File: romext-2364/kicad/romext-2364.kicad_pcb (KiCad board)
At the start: 2 copper layers, 58.4 x 58.4 mm, 2 parts, among them J1 2364, U1 2764

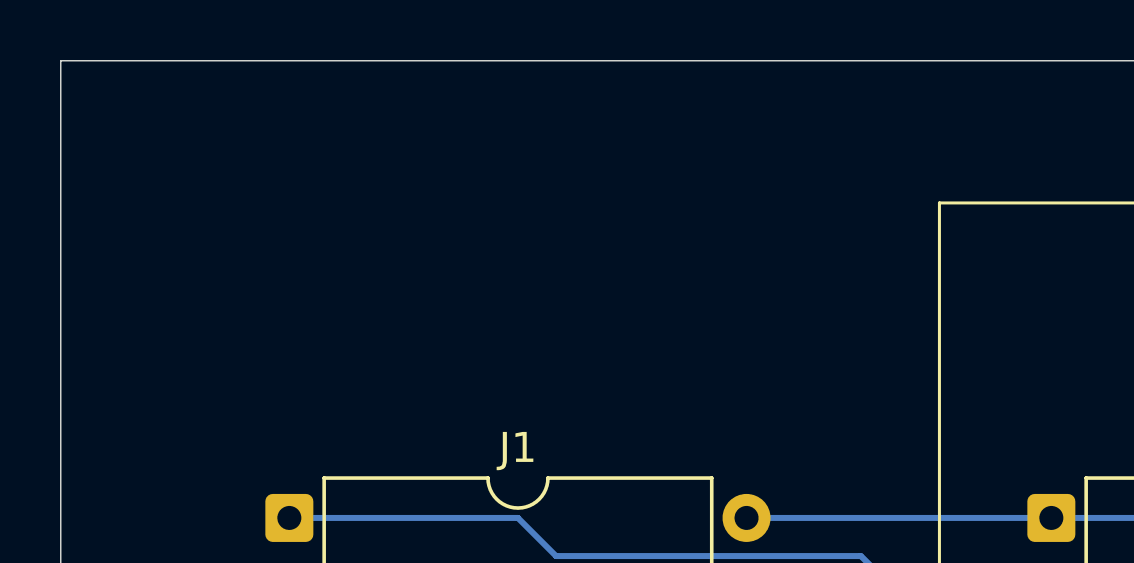
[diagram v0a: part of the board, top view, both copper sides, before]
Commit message: hwdev.romext-2364: Add name, url and revision to title block
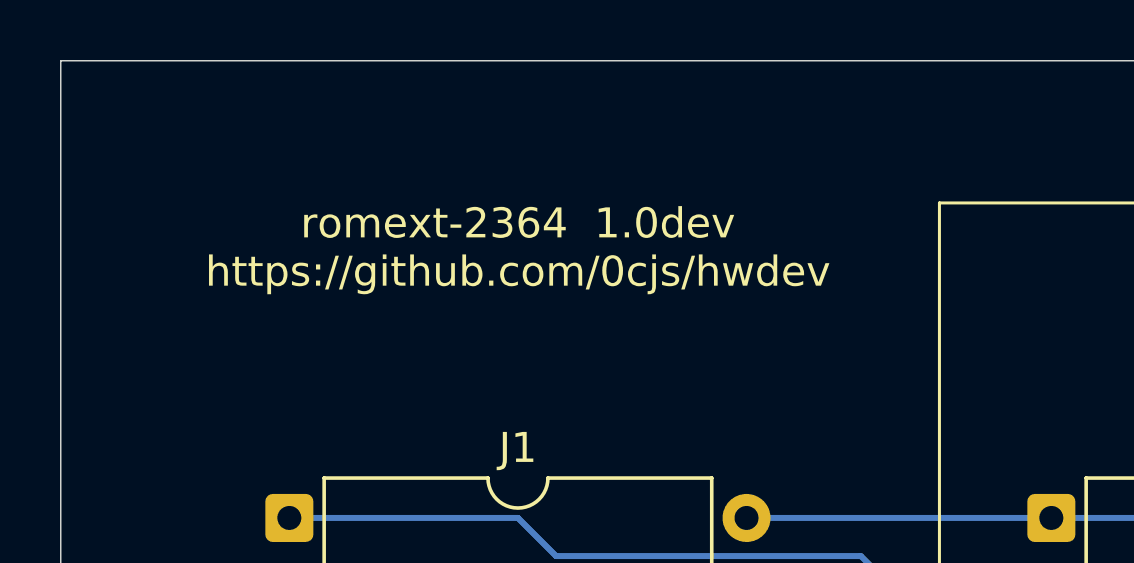
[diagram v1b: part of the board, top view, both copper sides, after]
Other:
- board text added: "${TITLE} ${REVISION} ${COMMENT1}"
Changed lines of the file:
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@@
 	)
 	(paper "A4")
+	(title_block
+		(title "romext-2364")
+		(rev "1.0dev")
+		(comment 1 "https://github.com/0cjs/hwdev")
+	)
 	(layers
 		(0 "F.Cu" signal)
@@
 		(layer "Edge.Cuts")
 	)
+	(gr_text "${TITLE}  ${REVISION}\n${COMMENT1}\n"
+		(at 109.22 43.18 0)
+		(layer "F.SilkS")
+		(effects
+			(font
+				(size 1 1)
+				(thickness 0.1)
+			)
+			(justify bottom)
+		)
+	)
 	(segment

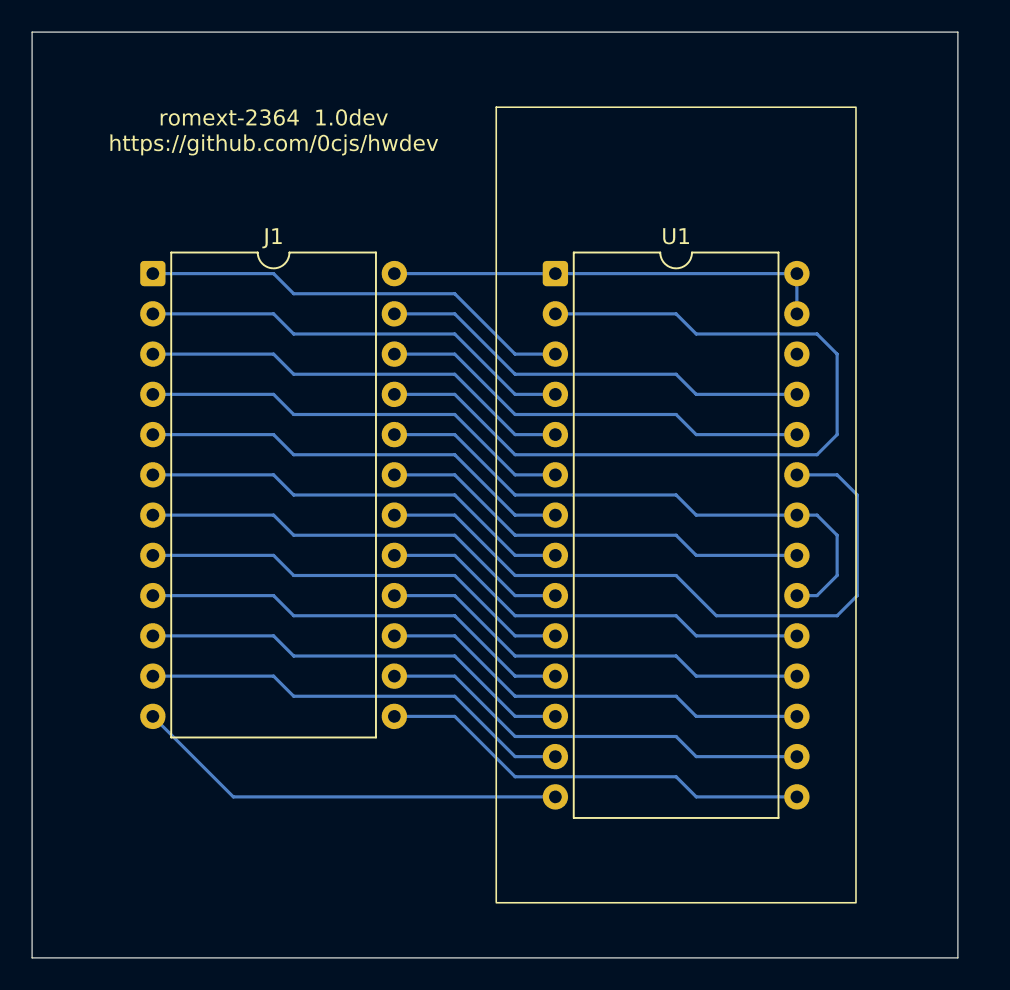
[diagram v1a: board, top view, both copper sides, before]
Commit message: romext-2364 pcb: Resize board; add mounting holes; move title
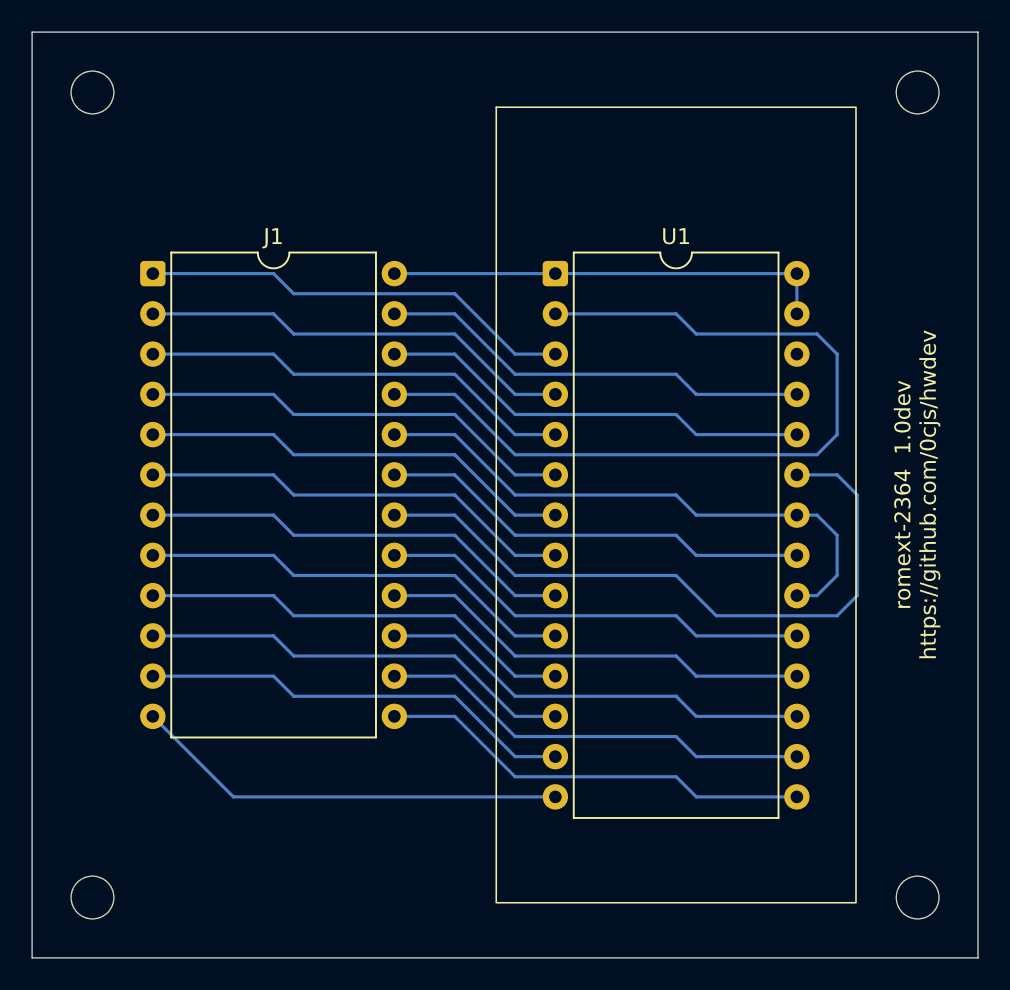
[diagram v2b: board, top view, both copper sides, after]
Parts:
- added REF**: MountingHole_2.7mm_M2.5, MountingHole:MountingHole_2.7mm_M2.5, F.Cu at (149.9, 39.4)
- added REF**: MountingHole_2.7mm_M2.5, MountingHole:MountingHole_2.7mm_M2.5, F.Cu at (149.9, 90.2)
- added REF**: MountingHole_2.7mm_M2.5, MountingHole:MountingHole_2.7mm_M2.5, F.Cu at (97.8, 90.2)
- added REF**: MountingHole_2.7mm_M2.5, MountingHole:MountingHole_2.7mm_M2.5, F.Cu at (97.8, 39.4)
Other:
- board size 58.4 x 58.4 mm -> 59.7 x 58.4 mm

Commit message: romext-2364 pcb: Change U1/2764 to use standard library ZIF footprint
Bumps PCB revision to 1-2dev.

The footprint was hard to find[1]; one has to turn off the footprint
filter to have it come up.

This updates the schematic as well, but just the footprint assignment
in it, so we don't need to bump the revision. (It does update the PDF,
however, because that contains the footprint info in the internal
Javascript for popups or whatever.)

[1]: https://forum.kicad.info/t/please-add-zif-to-the-descriptions-of-zero-insertion-force-sockets/62549/6
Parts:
- U1: footprint Package_DIP:DIP-28_W15.24mm -> Socket:DIP_Socket-28_W11.9_W12.7_W15.24_W17.78_W18.5_3M_228-1277-00-0602J

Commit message: romext-2364 pcb rev 2: Shrink board size slightly
There's room above and below J1/2364 for the mounting holes, so move
them there allowing us to bring in the left board edge by 5.08 mm (0.2").
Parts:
- moved REF** 5.08 mm to (102.9, 90.2)
- moved REF** 5.08 mm to (102.9, 39.4)
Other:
- board size 59.7 x 58.4 mm -> 54.6 x 58.4 mm
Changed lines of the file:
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@@
 	(title_block
 		(title "romext-2364")
-		(rev "1-2dev")
+		(rev "1-2")
 		(comment 1 "https://github.com/0cjs/hwdev")
 	)
@@
 	(footprint "MountingHole:MountingHole_2.7mm_M2.5"
 		(layer "F.Cu")
-		(at 97.79 90.17)
+		(at 102.87 90.17)
 		(descr "Mounting Hole 2.7mm, M2.5, no annular, generated by kicad-footprint-generator mountinghole.py")
 		(tags "mountinghole M2.5")
@@
 	(footprint "MountingHole:MountingHole_2.7mm_M2.5"
 		(layer "F.Cu")
-		(at 97.79 39.37)
+		(at 102.87 39.37)
 		(descr "Mounting Hole 2.7mm, M2.5, no annular, generated by kicad-footprint-generator mountinghole.py")
 		(tags "mountinghole M2.5")
@@
 	)
 	(gr_rect
-		(start 93.98 35.56)
+		(start 99.06 35.56)
 		(end 153.67 93.98)
 		(stroke
 			(width 0.05)
-			(type default)
+			(type solid)
 		)
 		(fill no)
